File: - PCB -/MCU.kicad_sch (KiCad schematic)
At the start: 2 parts

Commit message: PCB - board update + footprint/3d models export
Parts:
- U?: footprint ESP32 DOIT DevKit:MODULE_ESP32_DEVKIT_V1 B_Cu - PADS -> sumec_library:MODULE_ESP32_DEVKIT_V1 B_Cu - PADS and no mount holes
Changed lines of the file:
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@@
         )
         (path "/fc70a1a8-ed7c-4a0f-9b1a-f23293528385/11aa20d4-c4ff-49be-9179-c2911da50f67"
-          (reference "#PWR0102") (unit 1)
+          (reference "#PWR06") (unit 1)
         )
       )
@@
         )
         (path "/fc70a1a8-ed7c-4a0f-9b1a-f23293528385/11aa20d4-c4ff-49be-9179-c2911da50f67"
-          (reference "#PWR0103") (unit 1)
+          (reference "#PWR05") (unit 1)
         )
       )
@@
         )
         (path "/fc70a1a8-ed7c-4a0f-9b1a-f23293528385/11aa20d4-c4ff-49be-9179-c2911da50f67"
-          (reference "#PWR0101") (unit 1)
+          (reference "#PWR04") (unit 1)
         )
       )
@@
         )
         (path "/fc70a1a8-ed7c-4a0f-9b1a-f23293528385/11aa20d4-c4ff-49be-9179-c2911da50f67"
-          (reference "D1") (unit 1)
+          (reference "D2") (unit 1)
         )
       )
@@
       (effects (font (size 1.27 1.27)))
     )
-    (property "Footprint" "ESP32 DOIT DevKit:MODULE_ESP32_DEVKIT_V1 B_Cu - PADS" (at 151.13 102.87 0)
+    (property "Footprint" "sumec_library:MODULE_ESP32_DEVKIT_V1 B_Cu - PADS and no mount holes" (at 151.13 102.87 0)
       (effects (font (size 1.27 1.27)) (justify bottom) hide)
     )
@@
         )
         (path "/fc70a1a8-ed7c-4a0f-9b1a-f23293528385/11aa20d4-c4ff-49be-9179-c2911da50f67"
-          (reference "U12") (unit 1)
+          (reference "U1") (unit 1)
         )
       )

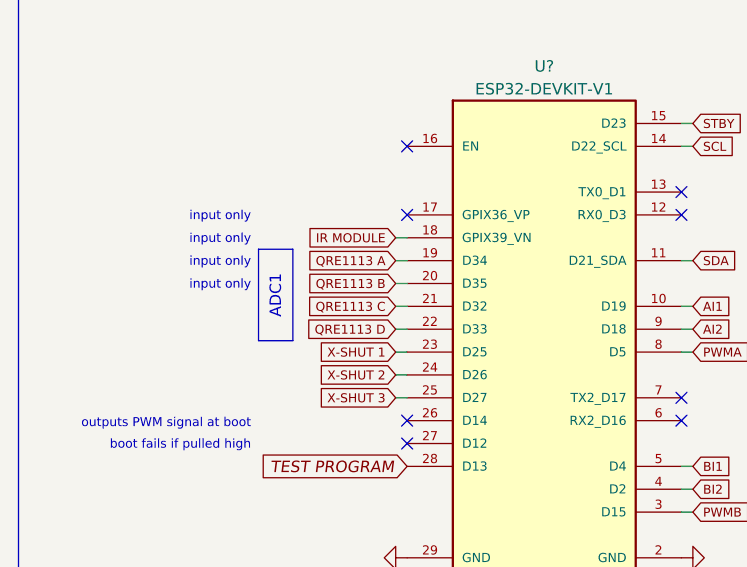
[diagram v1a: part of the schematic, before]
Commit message: PCB almost wired
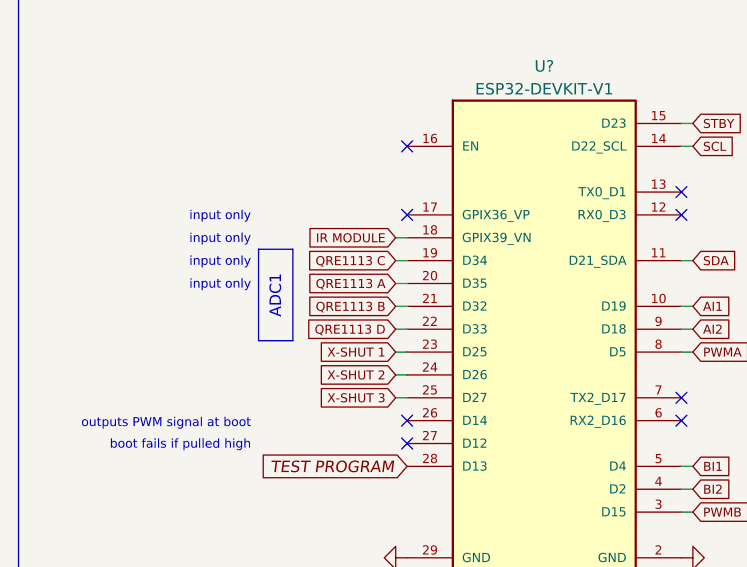
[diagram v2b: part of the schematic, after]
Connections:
- net QRE1113 A: now also U?.20 (D35); no longer U?.19 (D34)
- net QRE1113 B: now also U?.21 (D32); no longer U?.20 (D35)
- net QRE1113 C: now also U?.19 (D34); no longer U?.21 (D32)
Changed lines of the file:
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@@
+    (stroke (width 0) (type default))
+  )
+  (wire (pts (xy 80.01 106.68) (xy 81.28 106.68))
     (stroke (width 0) (type default))
   )
@@
     (stroke (width 0) (type default))
   )
-  (wire (pts (xy 80.01 106.68) (xy 81.28 106.68))
-    (stroke (width 0) (type default))
-  )
   (polyline (pts (xy 167.64 134.62) (xy 167.64 60.96))
     (stroke (width 0) (type default))
@@
     (stroke (width 0) (type default))
   )
+  (wire (pts (xy 80.01 96.52) (xy 81.28 96.52))
+    (stroke (width 0) (type default))
+  )
+  (polyline (pts (xy 38.1 63.5) (xy 38.1 134.62))
+    (stroke (width 0) (type default))
+  )
+  (wire (pts (xy 113.03 78.74) (xy 111.76 78.74))
+    (stroke (width 0) (type default))
+  )
   (wire (pts (xy 80.01 91.44) (xy 81.28 91.44))
-    (stroke (width 0) (type default))
-  )
-  (wire (pts (xy 80.01 96.52) (xy 81.28 96.52))
-    (stroke (width 0) (type default))
-  )
-  (polyline (pts (xy 38.1 63.5) (xy 38.1 134.62))
-    (stroke (width 0) (type default))
-  )
-  (wire (pts (xy 113.03 78.74) (xy 111.76 78.74))
     (stroke (width 0) (type default))
   )
@@
     )
   )
-  (global_label "QRE1113 C" (shape input) (at 80.01 96.52 180) (fields_autoplaced)
-    (effects (font (size 1 1)) (justify right))
-    (property "Intersheetrefs" "${INTERSHEET_REFS}" (at 69.3601 96.52 0)
+  (global_label "QRE1113 C" (shape input) (at 80.01 91.44 180) (fields_autoplaced)
+    (effects (font (size 1 1)) (justify right))
+    (property "Intersheetrefs" "${INTERSHEET_REFS}" (at 69.3601 91.44 0)
       (effects (font (size 1.27 1.27)) (justify right) hide)
     )
@@
     )
   )
-  (global_label "QRE1113 A" (shape input) (at 80.01 91.44 180) (fields_autoplaced)
-    (effects (font (size 1 1)) (justify right))
-    (property "Intersheetrefs" "${INTERSHEET_REFS}" (at 69.503 91.44 0)
+  (global_label "QRE1113 A" (shape input) (at 80.01 93.98 180) (fields_autoplaced)
+    (effects (font (size 1 1)) (justify right))
+    (property "Intersheetrefs" "${INTERSHEET_REFS}" (at 69.503 93.98 0)
       (effects (font (size 1.27 1.27)) (justify right) hide)
     )
@@
     )
   )
-  (global_label "QRE1113 B" (shape input) (at 80.01 93.98 180) (fields_autoplaced)
-    (effects (font (size 1 1)) (justify right))
-    (property "Intersheetrefs" "${INTERSHEET_REFS}" (at 69.3601 93.98 0)
-      (effects (font (size 1.27 1.27)) (justify right) hide)
-    )
+  (global_label "QRE1113 B" (shape input) (at 80.01 96.52 180) (fields_autoplaced)
+    (effects (font (size 1 1)) (justify right))
+    (property "Intersheetrefs" "${INTERSHEET_REFS}" (at 69.3601 96.52 0)
+      (effects (font (size 1.27 1.27)) (justify right) hide)
+    )

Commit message: PCB - Board update
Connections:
- net X-SHUT 1: now also U?.25 (D27); no longer U?.23 (D25)
- net X-SHUT 2: now also U?.23 (D25); no longer U?.24 (D26)
- net X-SHUT 3: now also U?.24 (D26); no longer U?.25 (D27)
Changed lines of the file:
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@@
     (effects (font (size 2 2)) (justify left bottom))
   )
-  (global_label "X-SHUT 2" (shape input) (at 80.01 104.14 180) (fields_autoplaced)
+  (global_label "X-SHUT 1" (shape input) (at 80.01 106.68 180) (fields_autoplaced)
+    (effects (font (size 1 1)) (justify right))
+    (property "Intersheetrefs" "${INTERSHEET_REFS}" (at 70.1697 106.68 0)
+      (effects (font (size 1.27 1.27)) (justify right) hide)
+    )
+  )
+  (global_label "X-SHUT 3" (shape input) (at 80.01 104.14 180) (fields_autoplaced)
     (effects (font (size 1 1)) (justify right))
     (property "Intersheetrefs" "${INTERSHEET_REFS}" (at 70.1697 104.14 0)
@@
     )
   )
-  (global_label "X-SHUT 1" (shape input) (at 80.01 101.6 180) (fields_autoplaced)
-    (effects (font (size 1 1)) (justify right))
-    (property "Intersheetrefs" "${INTERSHEET_REFS}" (at 70.1697 101.6 0)
-      (effects (font (size 1.27 1.27)) (justify right) hide)
-    )
-  )
   (global_label "BI2" (shape input) (at 113.03 116.84 0) (fields_autoplaced)
     (effects (font (size 1 1)) (justify left))
@@
     (property "Intersheetrefs" "${INTERSHEET_REFS}" (at 118.0798 78.74 0)
       (effects (font (size 1.27 1.27)) (justify left) hide)
+    )
+  )
+  (global_label "X-SHUT 2" (shape input) (at 80.01 101.6 180) (fields_autoplaced)
+    (effects (font (size 1 1)) (justify right))
+    (property "Intersheetrefs" "${INTERSHEET_REFS}" (at 70.1697 101.6 0)
+      (effects (font (size 1.27 1.27)) (justify right) hide)
     )
   )
@@
       (effects (font (size 1.27 1.27)) (justify right) hide)
     )
-  )
-  (global_label "X-SHUT 3" (shape input) (at 80.01 106.68 180) (fields_autoplaced)
-    (effects (font (size 1 1)) (justify right))
-    (property "Intersheetrefs" "${INTERSHEET_REFS}" (at 70.1697 106.68 0)
-      (effects (font (size 1.27 1.27)) (justify right) hide)
-    )

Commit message: PCB - LED Signal. board upd
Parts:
- added D1: RLED, LED_THT:LED_D5.0mm, symbol Device:LED
- added R1: 75, Resistor_THT:R_Axial_DIN0207_L6.3mm_D2.5mm_P10.16mm_Horizontal, symbol Device:R
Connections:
- net GND: now also D1.1 (K)
- net LED SIGNALISATION: now reaches U?.26 (D14)
- net LED SIGNALISATION: now also R1.2
- new net: D1.2 (A), R1.1
- no-connect marks 9 -> 8
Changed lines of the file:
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@@
   (no_connect (at 81.28 111.76))
   (no_connect (at 81.28 78.74))
-  (no_connect (at 81.28 109.22))
   (no_connect (at 111.76 83.82))
   (no_connect (at 111.76 127))
@@
     )
   )
+  (global_label "LED SIGNALISATION" (shape input) (at 81.28 109.22 180) (fields_autoplaced)
+    (effects (font (size 1 1)) (justify right))
+    (property "Intersheetrefs" "${INTERSHEET_REFS}" (at 64.7541 109.22 0)
+      (effects (font (size 1.27 1.27)) (justify right) hide)
+    )
+  )
   (global_label "SCL" (shape input) (at 113.03 78.74 0) (fields_autoplaced)
     (effects (font (size 1 1)) (justify left))
@@
     )
   )
+  (global_label "LED SIGNALISATION" (shape input) (at 66.04 73.66 0) (fields_autoplaced)
+    (effects (font (size 1 1)) (justify left))
+    (property "Intersheetrefs" "${INTERSHEET_REFS}" (at 82.5659 73.66 0)
+      (effects (font (size 1.27 1.27)) (justify left) hide)
+    )
+  )
   (global_label "QRE1113 B" (shape input) (at 80.01 96.52 180) (fields_autoplaced)
     (effects (font (size 1 1)) (justify right))
     (property "Intersheetrefs" "${INTERSHEET_REFS}" (at 69.3601 96.52 0)
       (effects (font (size 1.27 1.27)) (justify right) hide)
+    )
+  )
+  (symbol (lib_id "Device:LED") (at 54.61 73.66 0) (mirror x) (unit 1)
+    (in_bom yes) (on_board yes) (dnp no)
+    (property "Reference" "D1" (at 44.45 76.2 0)
+      (effects (font (size 1.27 1.27)))
+    )
+    (property "Value" "RLED" (at 44.45 73.66 0)
+      (effects (font (size 1.27 1.27)))
+    )
+    (property "Footprint" "LED_THT:LED_D5.0mm" (at 54.61 73.66 0)
+      (effects (font (size 1.27 1.27)) hide)
+    )
+    (property "Datasheet" "~" (at 54.61 73.66 0)
+      (effects (font (size 1.27 1.27)) hide)
+    )
+    (pin "1")
+    (pin "2")
+    (instances
+      (project "sumec"
+        (path "/fc70a1a8-ed7c-4a0f-9b1a-f23293528385/05a35bad-c108-46ad-8f95-76319a60a14f"
+          (reference "D1") (unit 1)
+        )
+        (path "/fc70a1a8-ed7c-4a0f-9b1a-f23293528385/11aa20d4-c4ff-49be-9179-c2911da50f67"
+          (reference "D1") (unit 1)
+        )
+      )
     )
   )
@@
         )
       )
+    )
+  )
+  (symbol (lib_id "Device:R") (at 62.23 73.66 90) (unit 1)
+    (in_bom yes) (on_board yes) (dnp no) (fields_autoplaced)
+    (property "Reference" "R1" (at 62.23 68.58 90)
+      (effects (font (size 1.27 1.27)))
+    )
+    (property "Value" "75" (at 62.23 71.12 90)
+      (effects (font (size 1.27 1.27)))
+    )
+    (property "Footprint" "Resistor_THT:R_Axial_DIN0207_L6.3mm_D2.5mm_P10.16mm_Horizontal" (at 62.23 75.438 90)
+      (effects (font (size 1.27 1.27)) hide)
+    )
+    (property "Datasheet" "~" (at 62.23 73.66 0)
+      (effects (font (size 1.27 1.27)) hide)
+    )
+    (pin "1")
+    (pin "2")
+    (instances
+      (project "sumec"
+        (path "/fc70a1a8-ed7c-4a0f-9b1a-f23293528385/11aa20d4-c4ff-49be-9179-c2911da50f67"
+          (reference "R1") (unit 1)
+        )
+      )
+    )
+  )
+  (symbol (lib_id "power:GND") (at 50.8 73.66 270) (unit 1)
+    (in_bom yes) (on_board yes) (dnp no) (fields_autoplaced)
+    (property "Reference" "#PWR03" (at 44.45 73.66 0)
+      (effects (font (size 1.27 1.27)) hide)
+    )
+    (property "Value" "GND" (at 46.99 74.295 90)
+      (effects (font (size 1.27 1.27)) (justify right) hide)
+    )
+    (property "Footprint" "" (at 50.8 73.66 0)
+      (effects (font (size 1.27 1.27)) hide)
+    )
+    (property "Datasheet" "" (at 50.8 73.66 0)
+      (effects (font (size 1.27 1.27)) hide)
+    )
+    (pin "1")
+    (instances
+      (project "sumec"
+        (path "/fc70a1a8-ed7c-4a0f-9b1a-f23293528385/05a35bad-c108-46ad-8f95-76319a60a14f"
+          (reference "#PWR03") (unit 1)
+        )
+        (path "/fc70a1a8-ed7c-4a0f-9b1a-f23293528385/11aa20d4-c4ff-49be-9179-c2911da50f67"
+          (reference "#PWR03") (unit 1)
+        )
+      )

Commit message: PCB sumec THT update
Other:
- company: (none) -> SPŠ NA PROSEKU
- title: (none) -> SUMEC THT
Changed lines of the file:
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@@
 (kicad_sch (version 20230121) (generator eeschema)
   (paper "A4")
+  (title_block
+    (title "SUMEC THT")
+    (company "SPŠ NA PROSEKU")
+  )
   (no_connect (at 81.28 86.36))
   (no_connect (at 111.76 86.36))
